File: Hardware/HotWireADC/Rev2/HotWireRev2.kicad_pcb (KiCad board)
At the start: 2 copper layers, 87 x 97.2 mm, 50 parts, among them CON1 BARREL_JACK, P1 BNC, P2 BNC, P3 BNC, P4 BNC, P5 CONN_02X06, P6 BNC, SW1 SW_PUSH_SMALL, U1 OPA320, U2 OPA320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

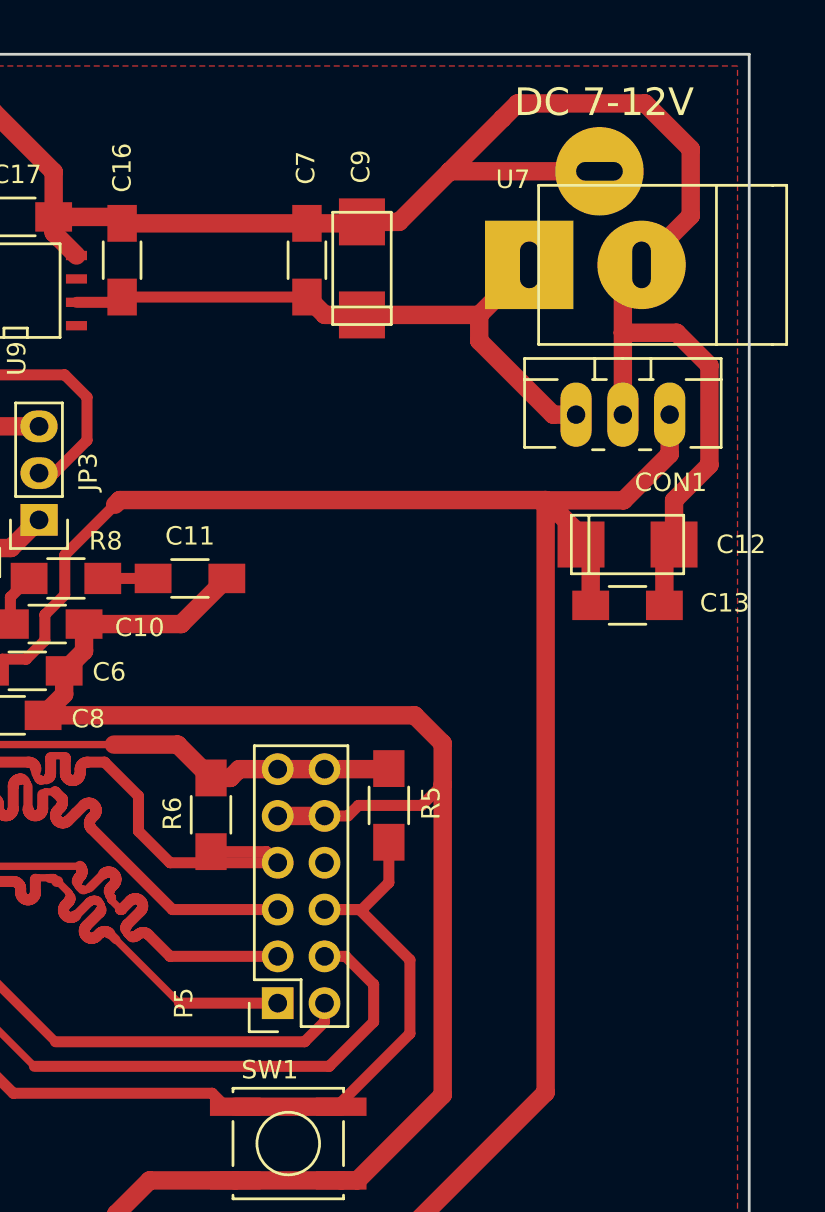
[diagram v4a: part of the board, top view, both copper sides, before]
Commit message: implemented new DC jack footprint
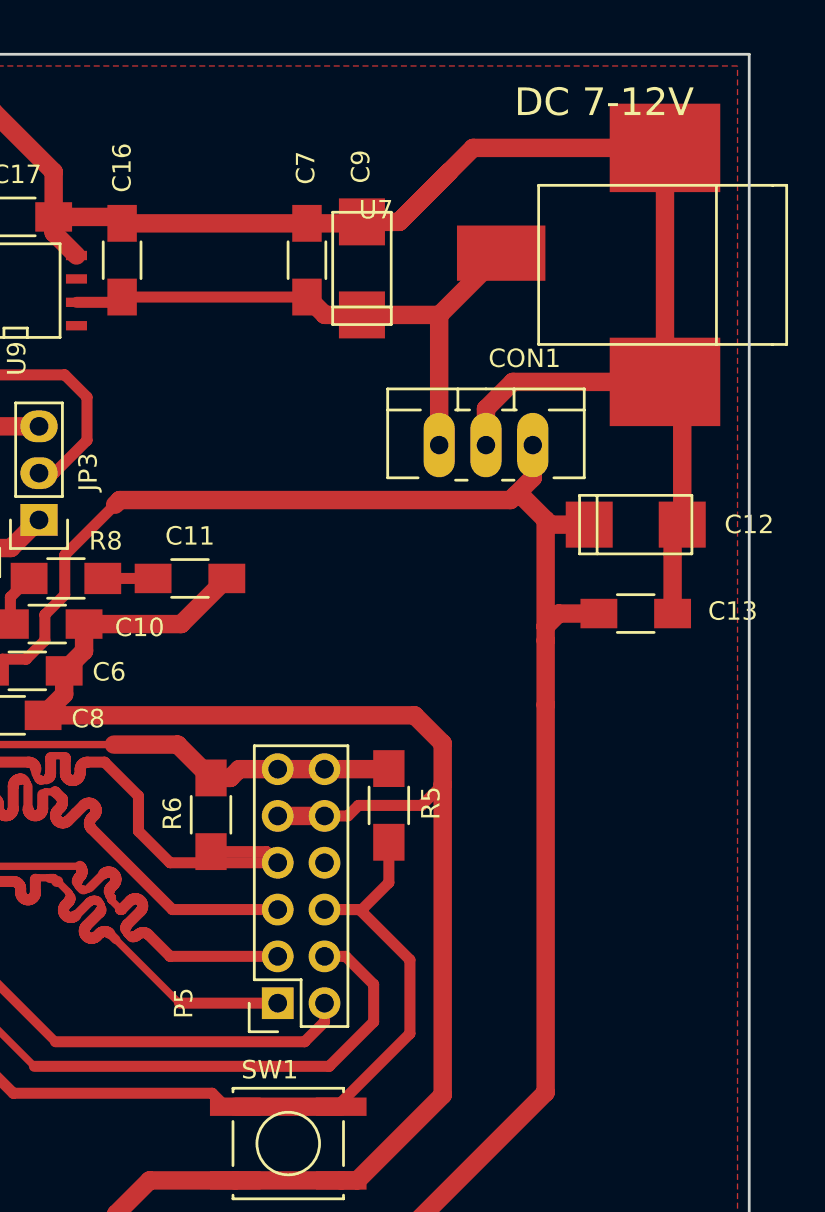
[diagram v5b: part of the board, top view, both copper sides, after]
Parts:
- C9: value 10u -> 10u tant
- CON1: footprint Connect:JACK_ALIM -> CustomFootprints:JACK_SMD
- R10: value 0.5 -> 0.5R
- moved U7 7.61 mm to (187.6, 59.1)
- moved C12 1.17 mm to (195.8, 63.4)
- moved C13 0.63 mm to (195.8, 68.2)
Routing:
- net +5VA: track 650.8 -> 623.9 mm
- net VCC: track 46.8 -> 33.4 mm
- net GNDA: track 653.7 -> 647.4 mm

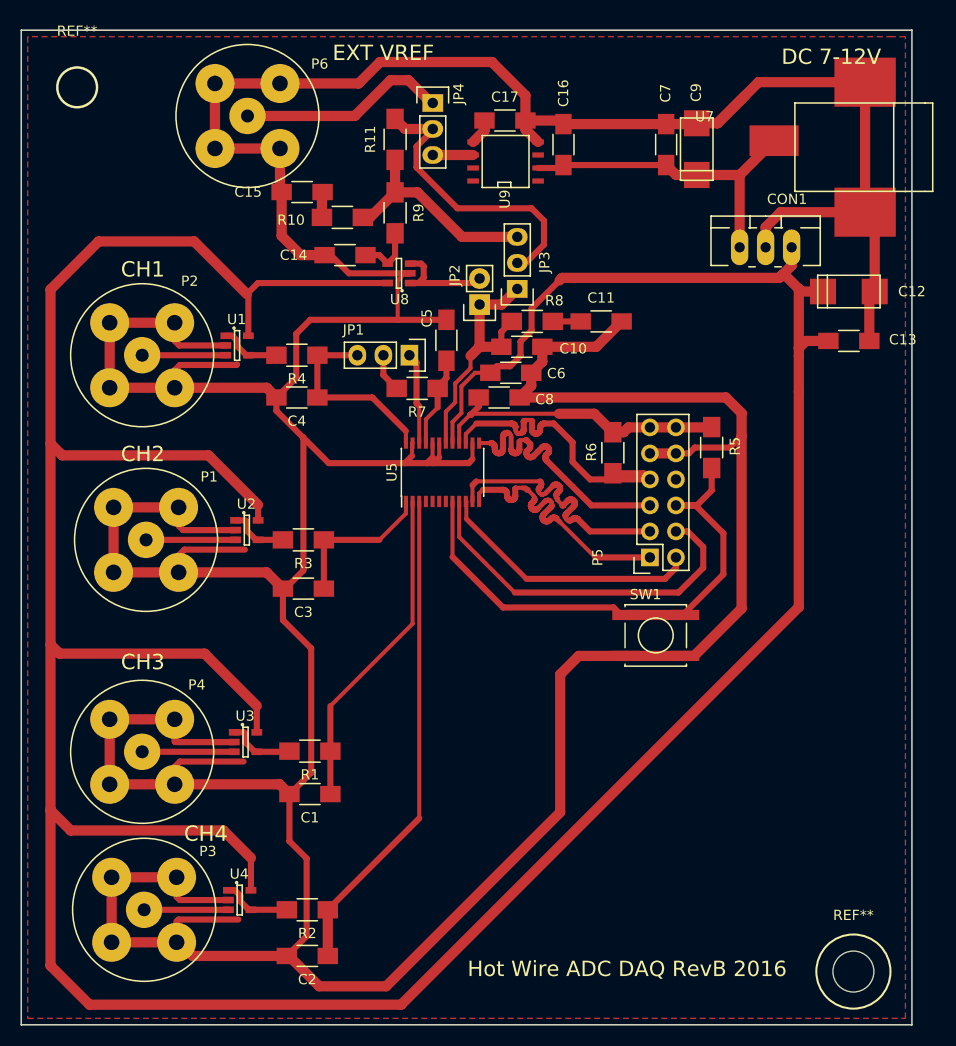
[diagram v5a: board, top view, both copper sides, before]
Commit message: added extra marks and alignment to PCB for silkscreen
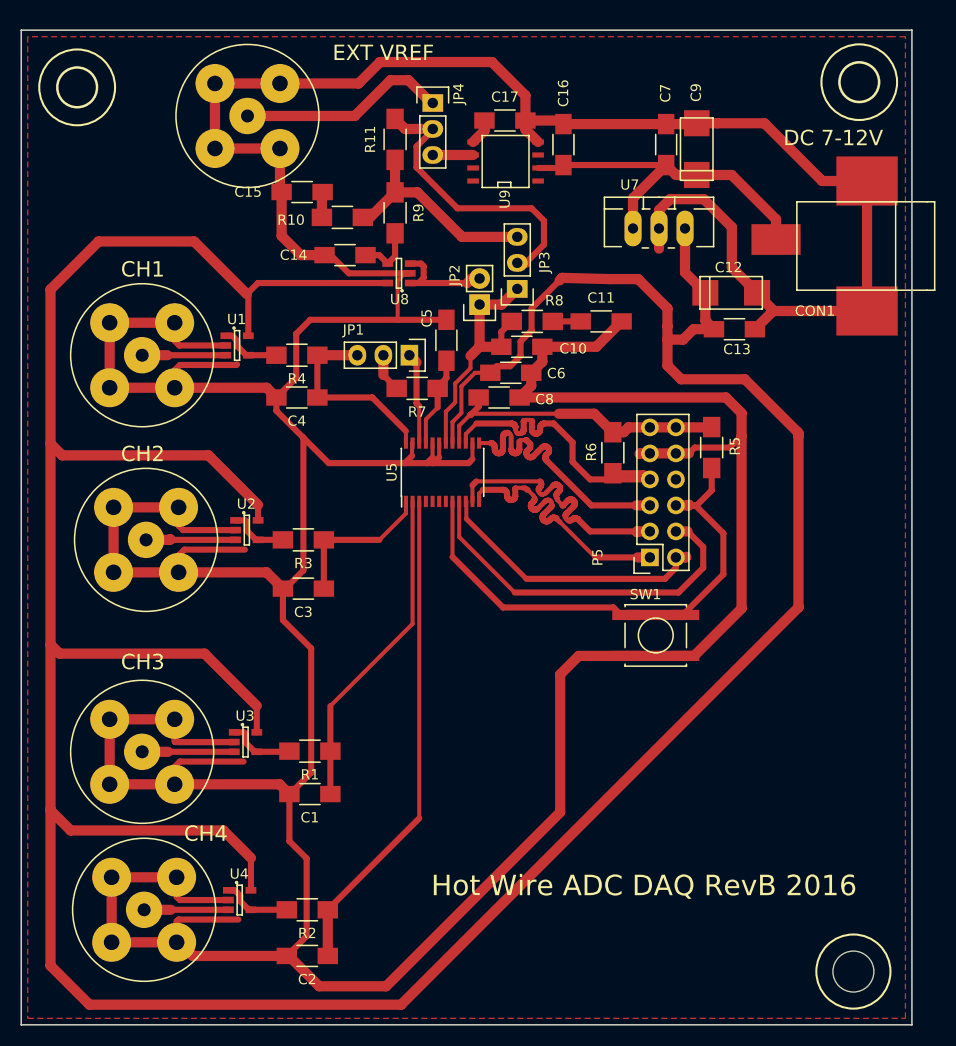
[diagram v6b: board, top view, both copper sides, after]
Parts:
- added REF**: MountingHole_4mm, Mounting_Holes:MountingHole_4mm, F.Cu at (196.8, 42.9)
- moved C12 11.5 mm to (184.3, 63.5)
- moved C13 11.2 mm to (184.6, 67.1)
- moved U7 10.6 mm to (177.2, 57.2)
- moved CON1 9.65 mm to (196.3, 58.9)
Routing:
- net +5VA: track 623.9 -> 605.1 mm
- net VCC: track 33.4 -> 36.4 mm
- net GNDA: track 647.4 -> 650.1 mm
- net Net-(JP2-Pad2): track 10.2 -> 11.6 mm
- net /SDI: track 26.3 -> 27.5 mm
- net /SCLK: track 26.1 -> 27.2 mm
- net Net-(JP1-Pad1): track 8.98 -> 9.97 mm
- net Net-(JP3-Pad2): track 28.8 -> 29.6 mm
